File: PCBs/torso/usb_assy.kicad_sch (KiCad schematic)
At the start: 5 parts, among them J1 USB_B_Micro

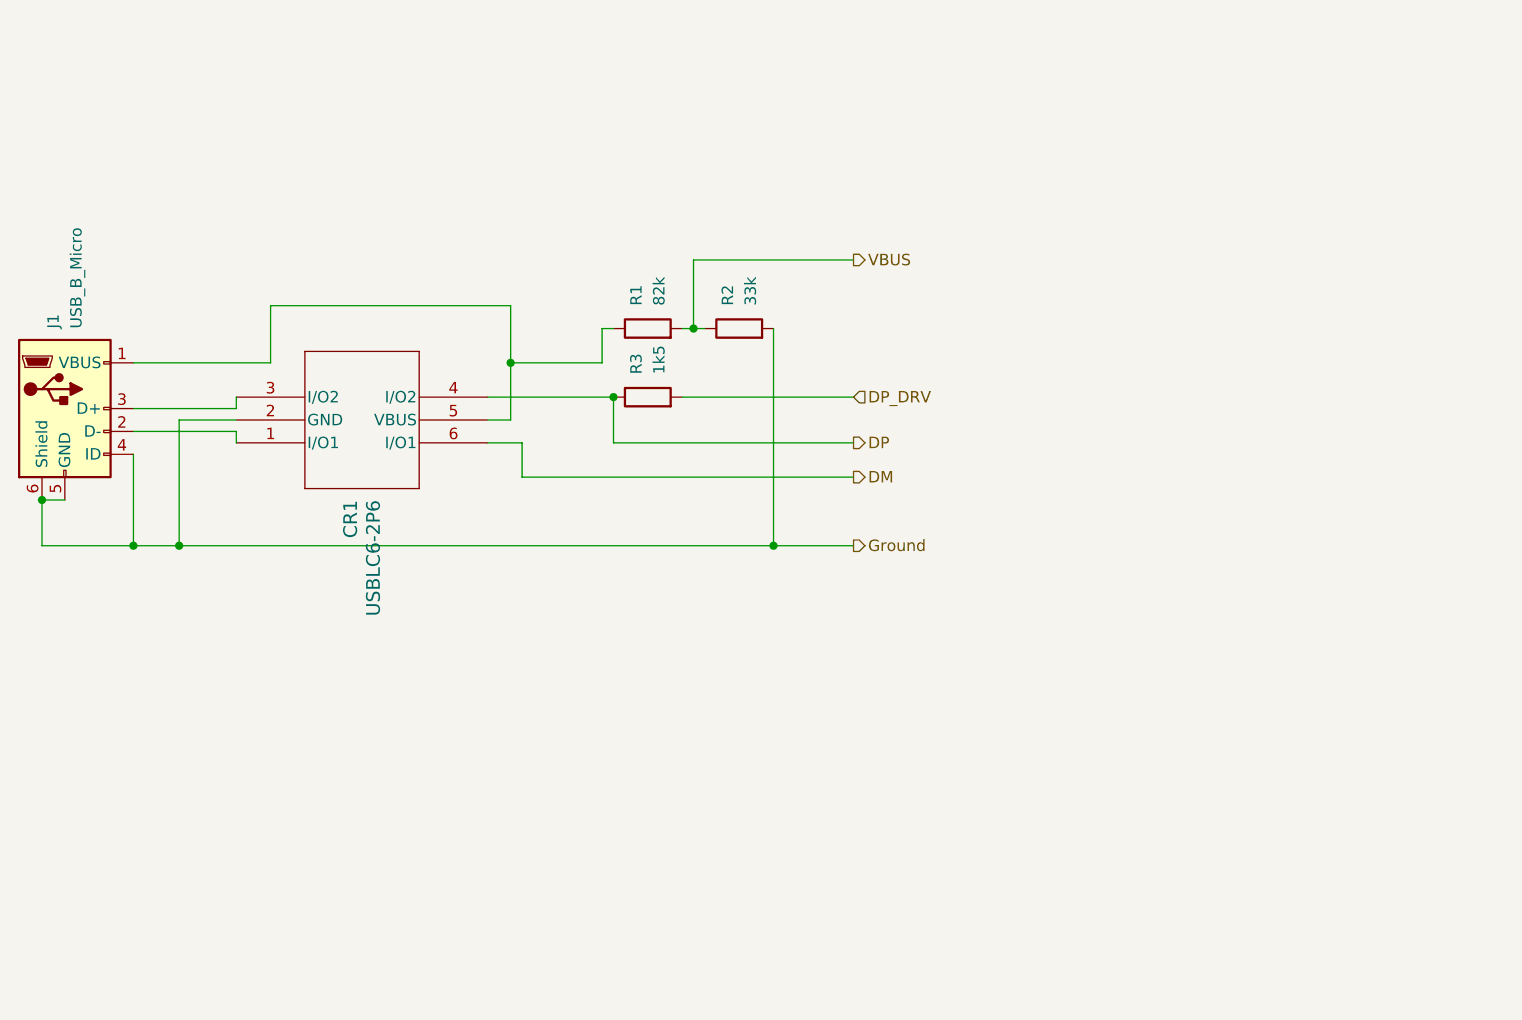
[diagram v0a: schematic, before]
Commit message: Torso all but complete, making bogie before checking the last mark
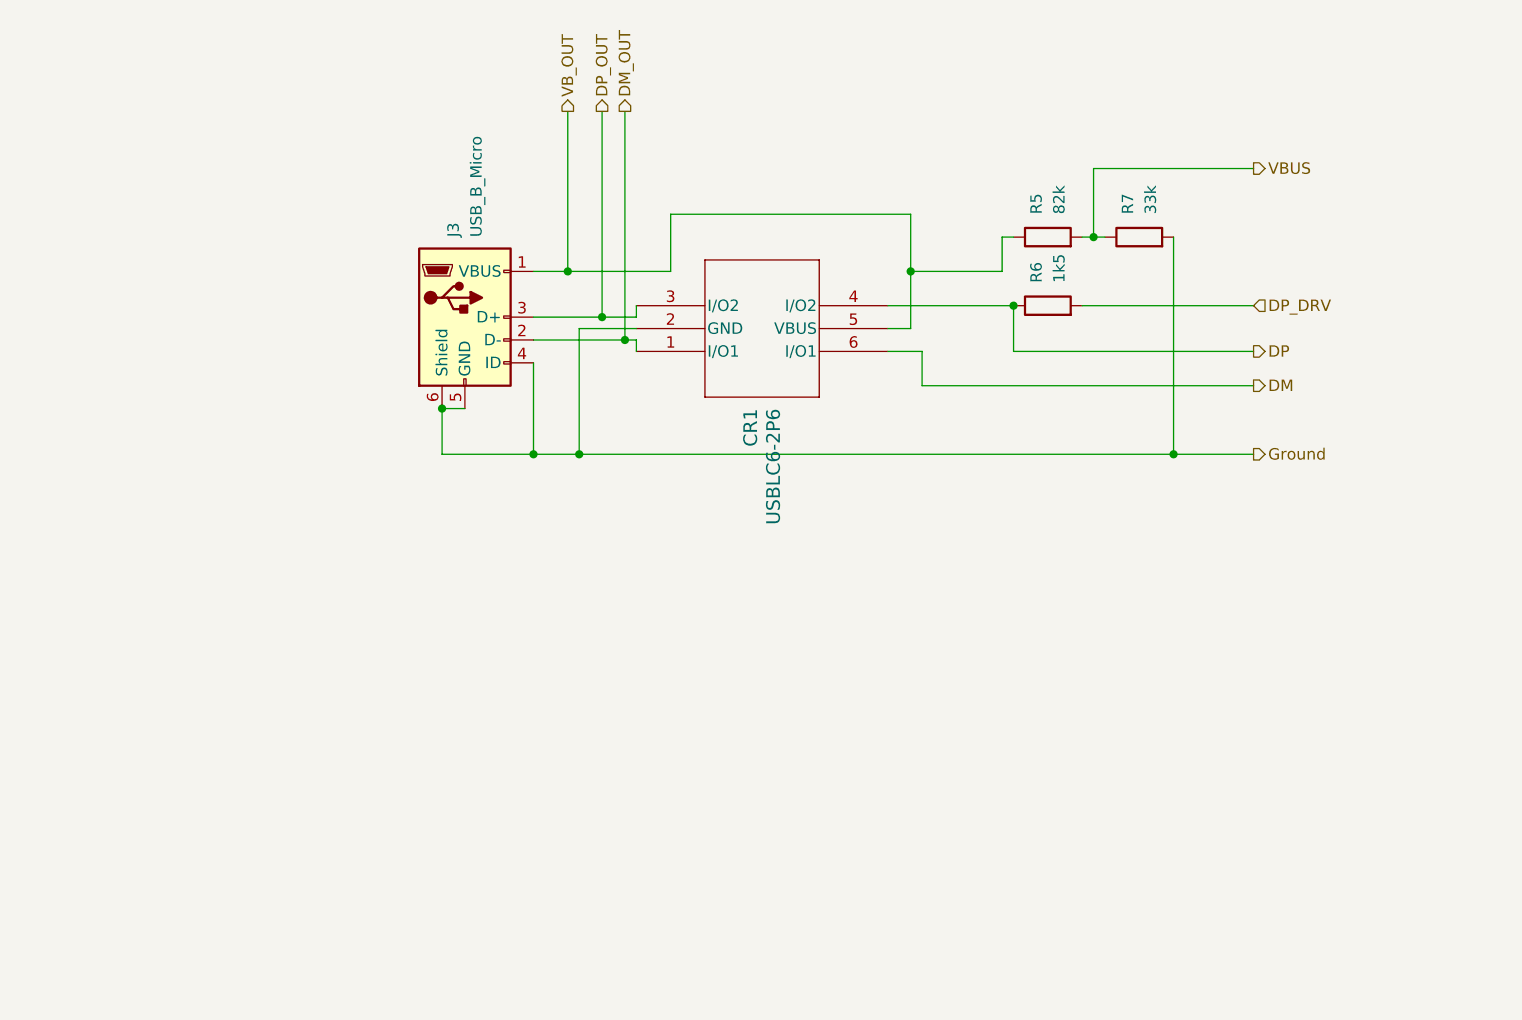
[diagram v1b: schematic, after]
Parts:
- removed J1: USB_B_Micro, Connector_USB:USB_Micro-B_Molex-105017-0001, symbol Connector:USB_B_Micro
- removed R1: 82k, Resistor_SMD:R_0603_1608Metric_Pad0.98x0.95mm_HandSolder, symbol Device:R
- removed R2: 33k, Resistor_SMD:R_0603_1608Metric_Pad0.98x0.95mm_HandSolder, symbol Device:R
- removed R3: 1k5, Resistor_SMD:R_0603_1608Metric_Pad0.98x0.95mm_HandSolder, symbol Device:R
- added J3: USB_B_Micro, Connector_USB:USB_Micro-B_Molex-105017-0001, symbol Connector:USB_B_Micro
- added R5: 82k, Resistor_SMD:R_0603_1608Metric_Pad0.98x0.95mm_HandSolder, symbol Device:R
- added R6: 1k5, Resistor_SMD:R_0603_1608Metric_Pad0.98x0.95mm_HandSolder, symbol Device:R
- added R7: 33k, Resistor_SMD:R_0603_1608Metric_Pad0.98x0.95mm_HandSolder, symbol Device:R
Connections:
- net DP: now also R6.1
- net DP_DRV: now also R6.2
- net Ground: now also J3.4 (ID), J3.5 (GND), J3.6 (Shield), R7.2
- net VBUS: now also R5.2, R7.1
- net VB_OUT: now reaches CR1.5 (VBUS)
- net VB_OUT: now also J3.1 (VBUS), R5.1
- net DM_OUT: now reaches CR1.1 (I/O1)
- net DM_OUT: now also J3.2 (D-)
- net DP_OUT: now reaches CR1.3 (I/O2)
- net DP_OUT: now also J3.3 (D+)
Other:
- title: USB connector assembly -> (none)

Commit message: Added pcb pdfs
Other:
- moved on the sheet: CR1, J3, R5, R6, R7

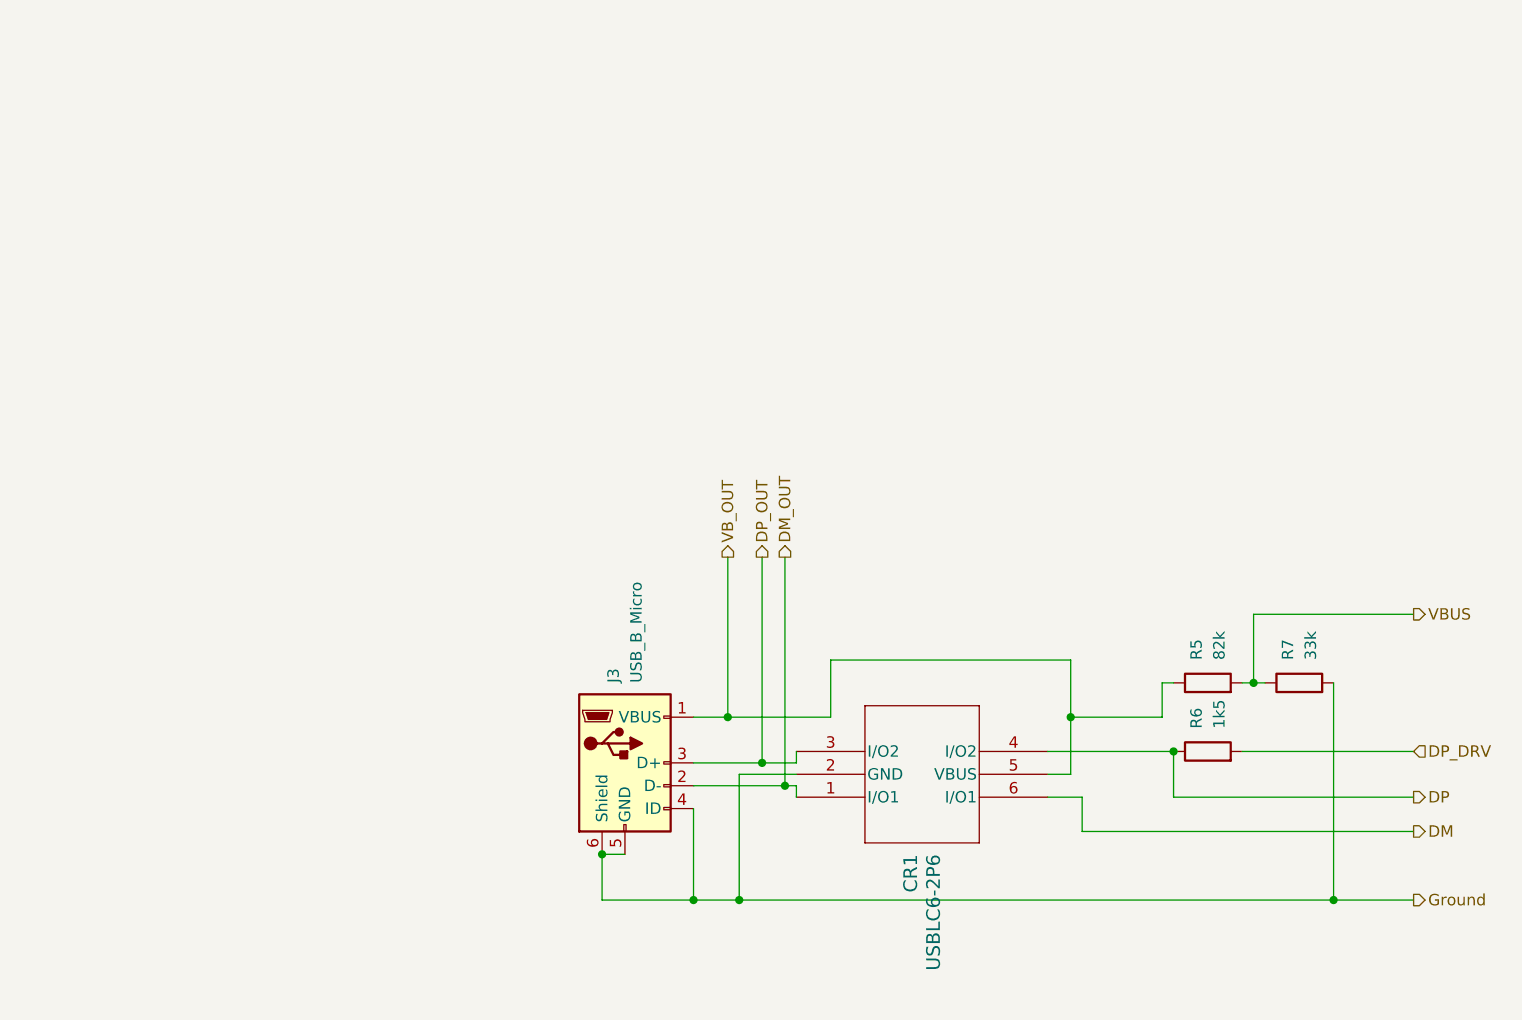
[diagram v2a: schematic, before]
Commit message: merged changes from timertests, mostly documentation and such. Did not add tim6 config
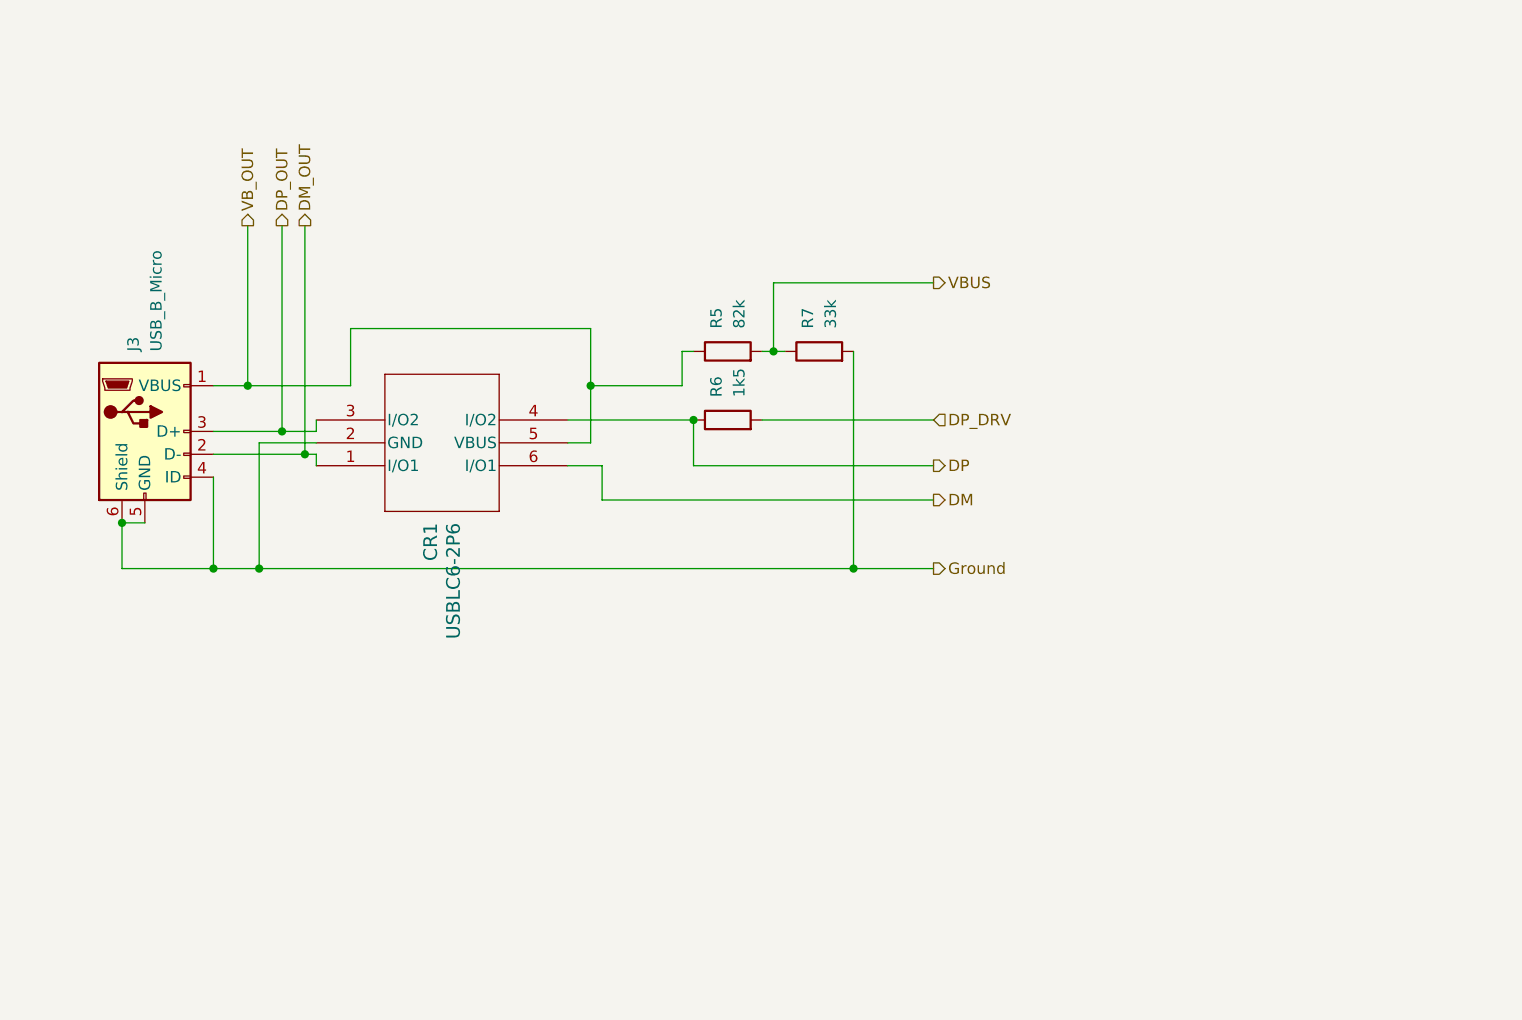
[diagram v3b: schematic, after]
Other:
- title: (none) -> USB assembly
- moved on the sheet: CR1, J3, R5, R6, R7
